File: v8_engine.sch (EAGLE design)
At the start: 79 parts, among them IC1 4024N, IC2 4046N, IC3 40106N, IC4 LM358N, IC5 LM358N, IC6 LM358N

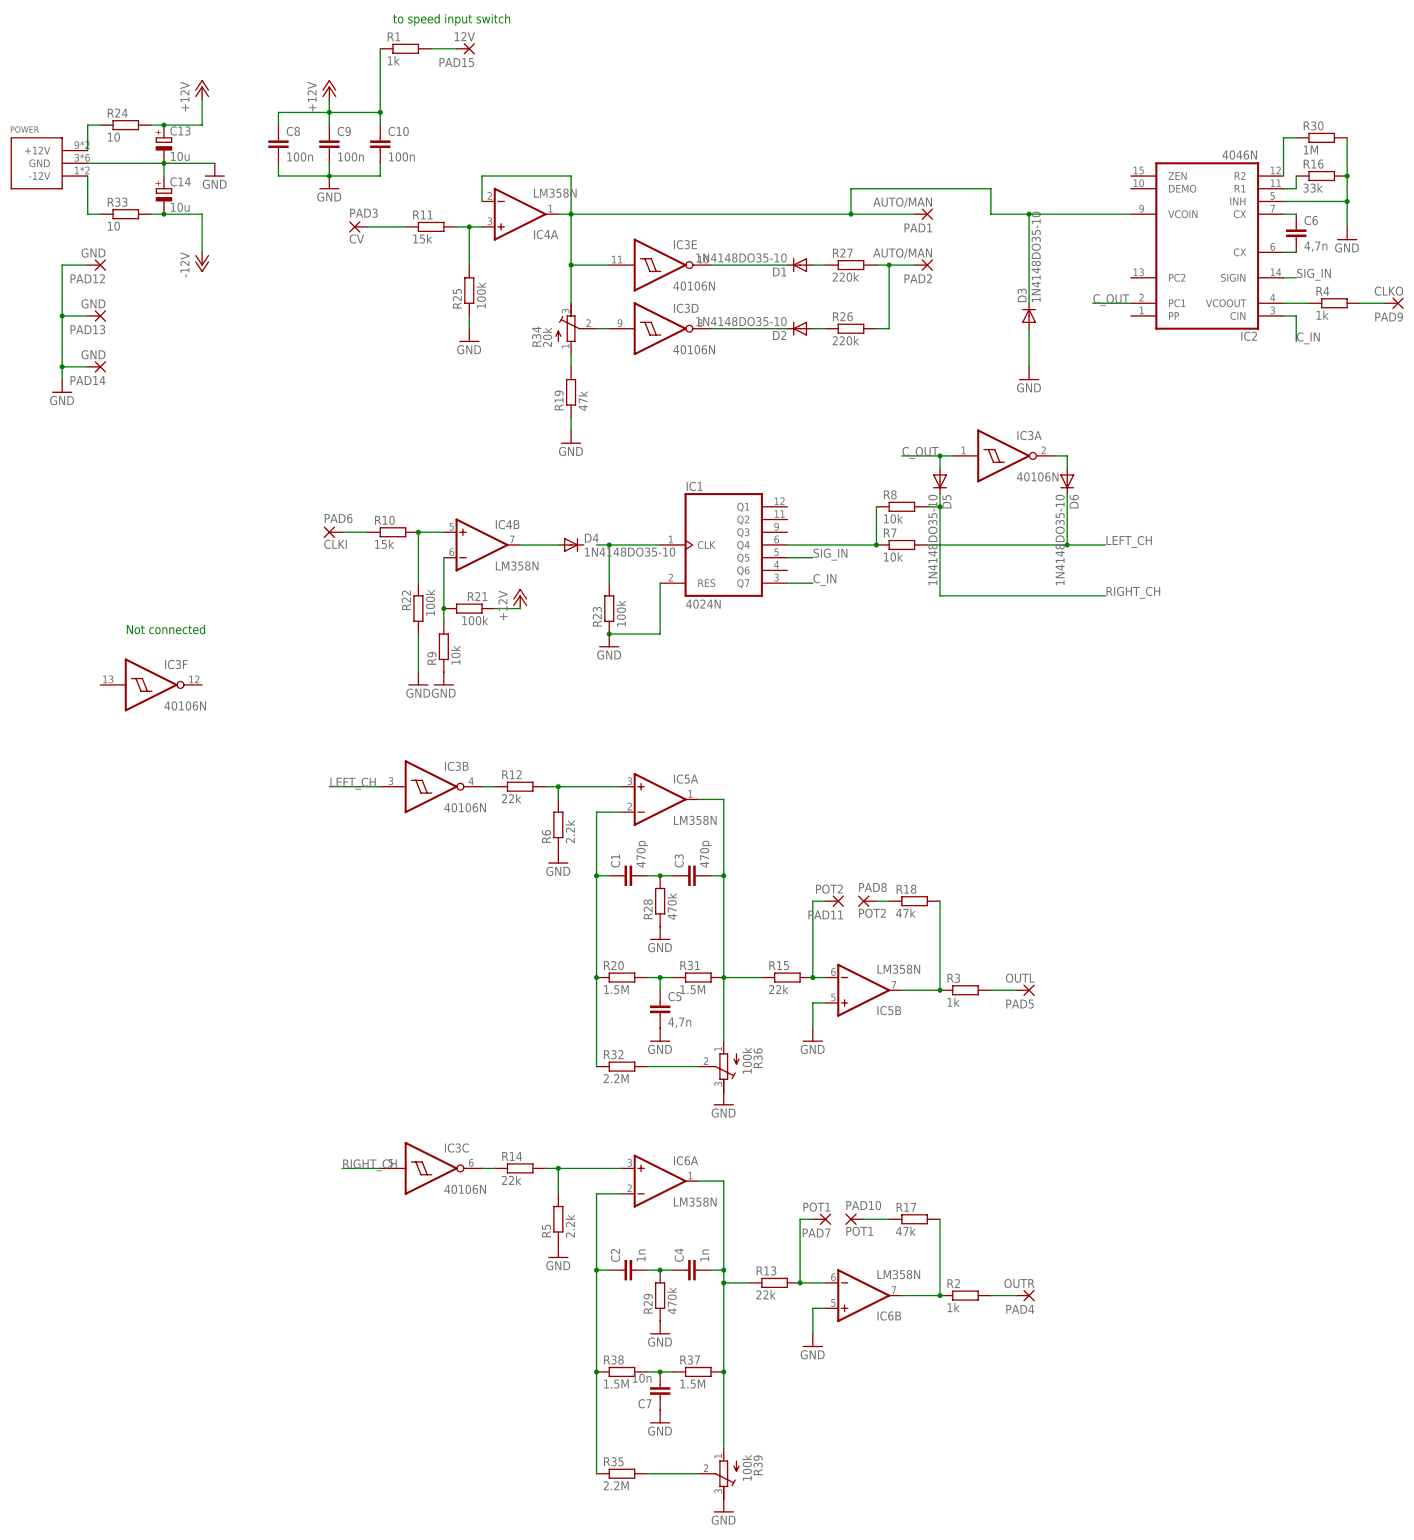
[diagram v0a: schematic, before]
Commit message: Rearrange all components on the PCB
- Arrange components on pcb to make some kind of sense.
- Change size of board and add screw holes for m3 screw.
	- Note that size/layout might not be final.
- Invoke all ICs to connect them to +12V -12V and GND nets.
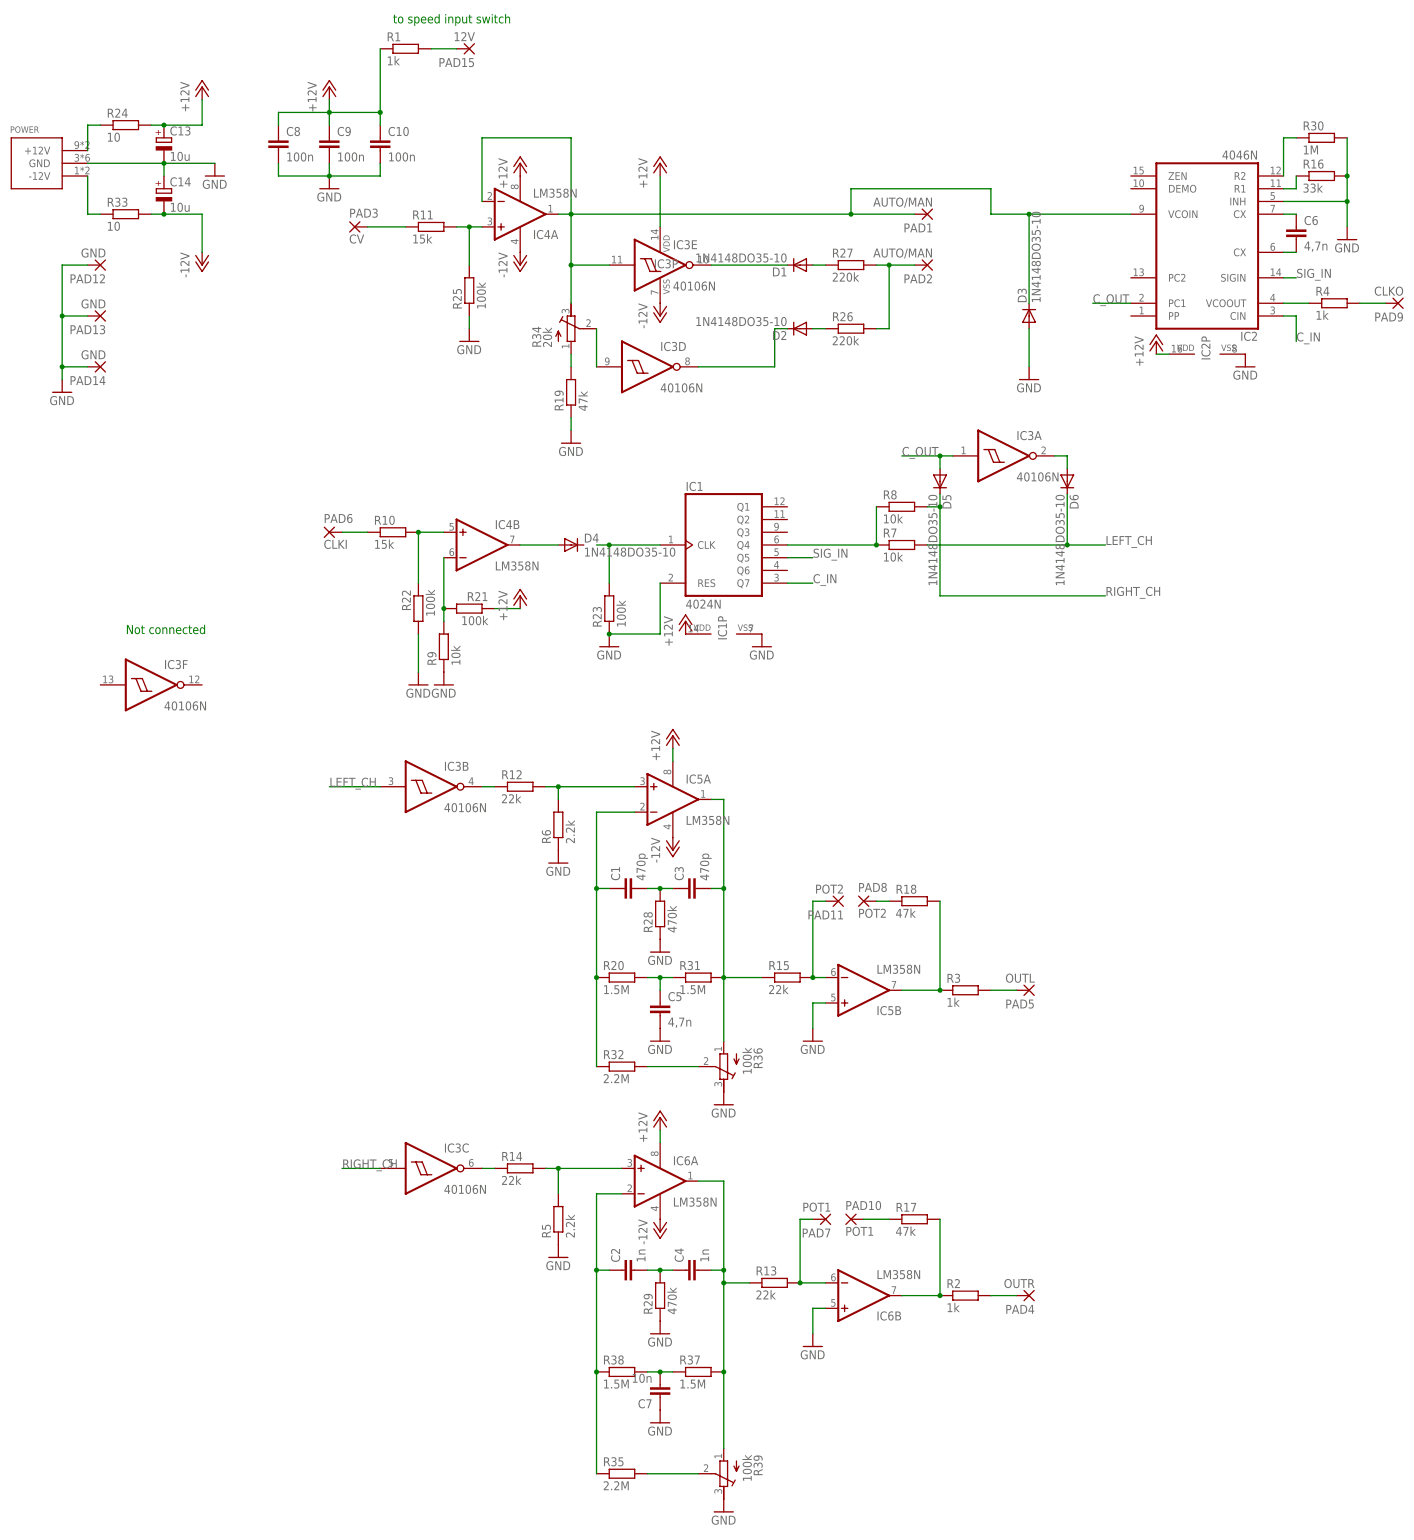
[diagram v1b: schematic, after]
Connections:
- net +12V: now also IC1P.VDD, IC2P.VDD, IC3P.VDD, IC4P.V+, IC5P.V+, IC6P.V+
- net -12V: now also IC3P.VSS, IC4P.V-, IC5P.V-, IC6P.V-
- net GND: now also IC1P.VSS, IC2P.VSS
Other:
- moved on the sheet: C1, C3, IC3D, IC5A, R28

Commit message: Change big ICs from DIL to SO make board smaller and start routing
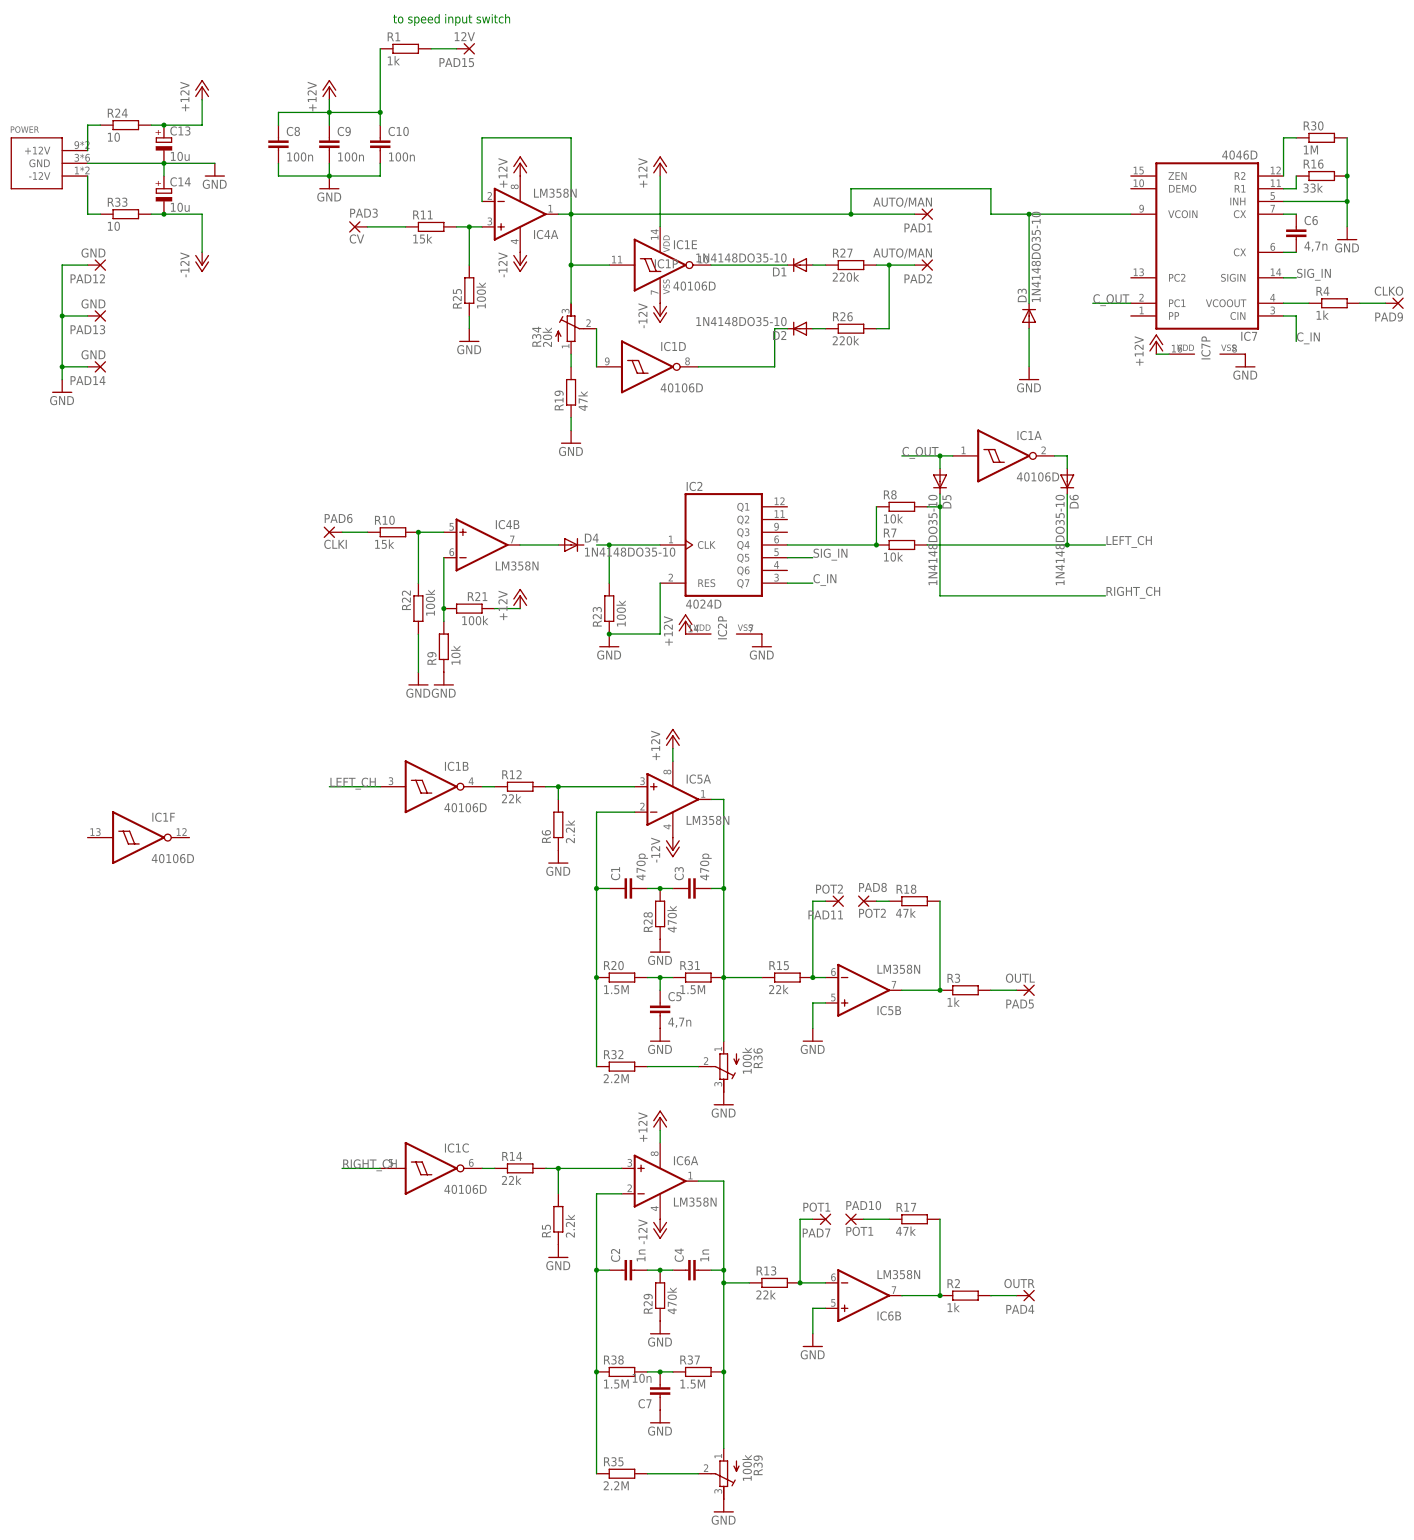
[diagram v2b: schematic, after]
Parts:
- removed IC3: 40106N, 40xx:40106N
- added IC7: 4046D, 40xx:4046D
- IC1: value 4024N -> 40106D; device 40xx:4024N -> 40xx:40106D
- IC2: value 4046N -> 4024D; device 40xx:4046N -> 40xx:4024D
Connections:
- net +12V: now also IC7P.VDD; no longer IC3P.VDD
- net -12V: now also IC1P.VSS; no longer IC3P.VSS
- net C_IN: now also IC2A.Q7, IC7A.CIN; no longer IC1A.Q7, IC2A.CIN
- net C_OUT: now also IC1A.I, IC7A.PC1; no longer IC2A.PC1, IC3A.I
- net GND: now also IC2A.RES, IC7A.INH, IC7P.VSS; no longer IC1A.RES, IC1P.VSS, IC2A.INH
- net LEFT_CH: now also IC1B.I; no longer IC3B.I
- net N$1: now also IC7A.VCOOUT; no longer IC2A.VCOOUT
- net N$10: now also IC1D.I; no longer IC3D.I
- net N$16: now also IC7A.CX@2; no longer IC2A.CX@2
- net N$17: now also IC7A.CX@1; no longer IC2A.CX@1
- net N$18: now also IC7A.R1; no longer IC2A.R1
- net N$19: now also IC7A.R2; no longer IC2A.R2
- net N$21: now also IC2A.CLK; no longer IC1A.CLK
- net N$22: now also IC2A.Q4; no longer IC1A.Q4
- net N$24: now also IC1B.O; no longer IC3B.O
- net N$26: now also IC1A.O; no longer IC3A.O
- net N$41: now also IC1C.O; no longer IC3C.O
- net N$48: now also IC1E.I, IC7A.VCOIN; no longer IC2A.VCOIN, IC3E.I
- net N$6: now also IC1D.O; no longer IC3D.O
- net N$8: now also IC1E.O; no longer IC3E.O
- net RIGHT_CH: now also IC1C.I; no longer IC3C.I
- net SIG_IN: now also IC2A.Q5, IC7A.SIGIN; no longer IC1A.Q5, IC2A.SIGIN
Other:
- note removed: "Not connected"
- moved on the sheet: IC1P, IC2P

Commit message: Clean up silk screen and fix issues
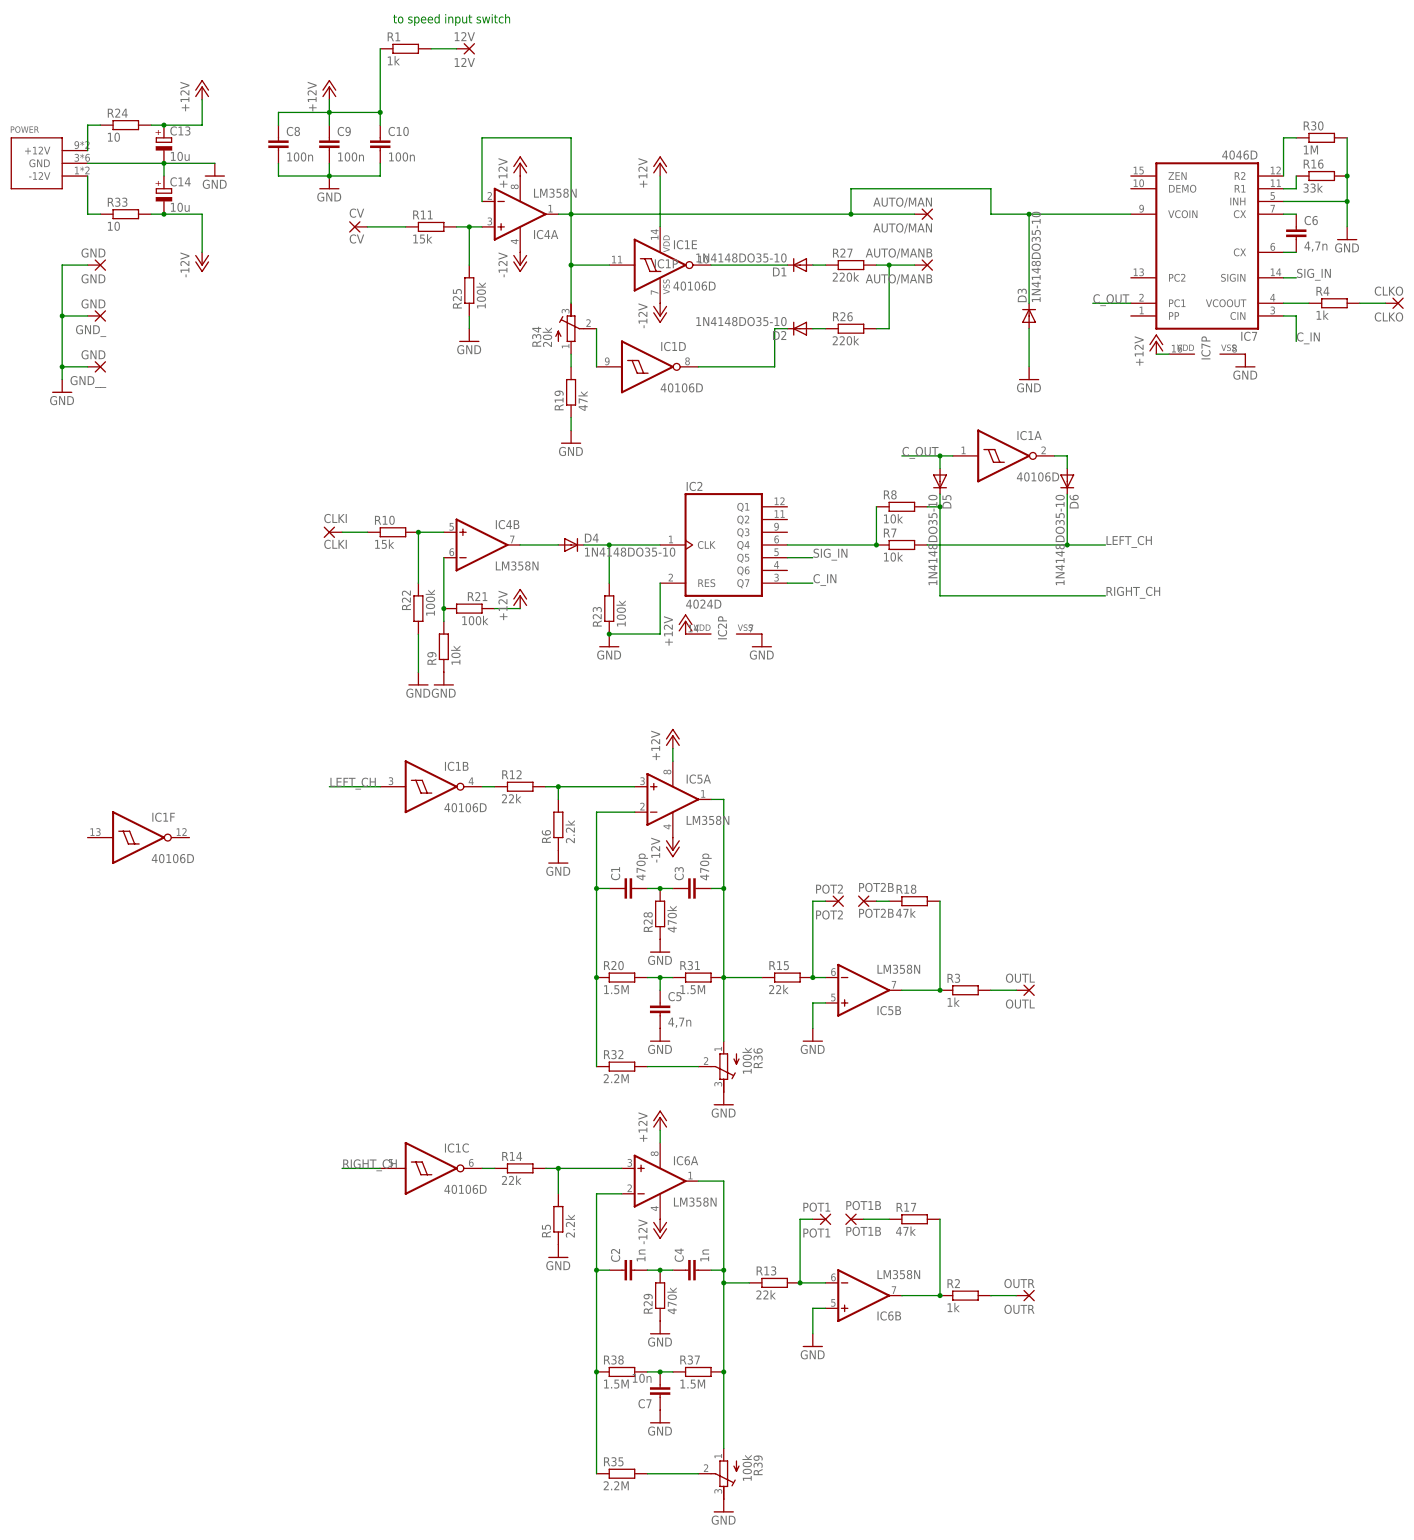
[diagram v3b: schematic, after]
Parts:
- AUTO/MANB: value AUTO/MAN -> AUTO/MANB
- POT1B: value POT1 -> POT1B
- POT2B: value POT2 -> POT2B
- renumbered PAD1 to AUTO/MAN, PAD10 to POT1B, PAD11 to POT2, PAD12 to GND, PAD13 to GND_, PAD14 to GND__, PAD15 to 12V, PAD2 to AUTO/MANB, PAD3 to CV, PAD4 to OUTR, PAD5 to OUTL, PAD6 to CLKI, PAD7 to POT1, PAD8 to POT2B, PAD9 to CLKO
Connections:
- net N$21: now also D4.C
